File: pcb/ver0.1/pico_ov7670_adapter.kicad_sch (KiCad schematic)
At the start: 11 parts, among them J1 Conn_02x06_Odd_Even, SW1 SW_Push, U1 CAMERA-OV7670, U2 RASPBERRY_PI_PICO_W

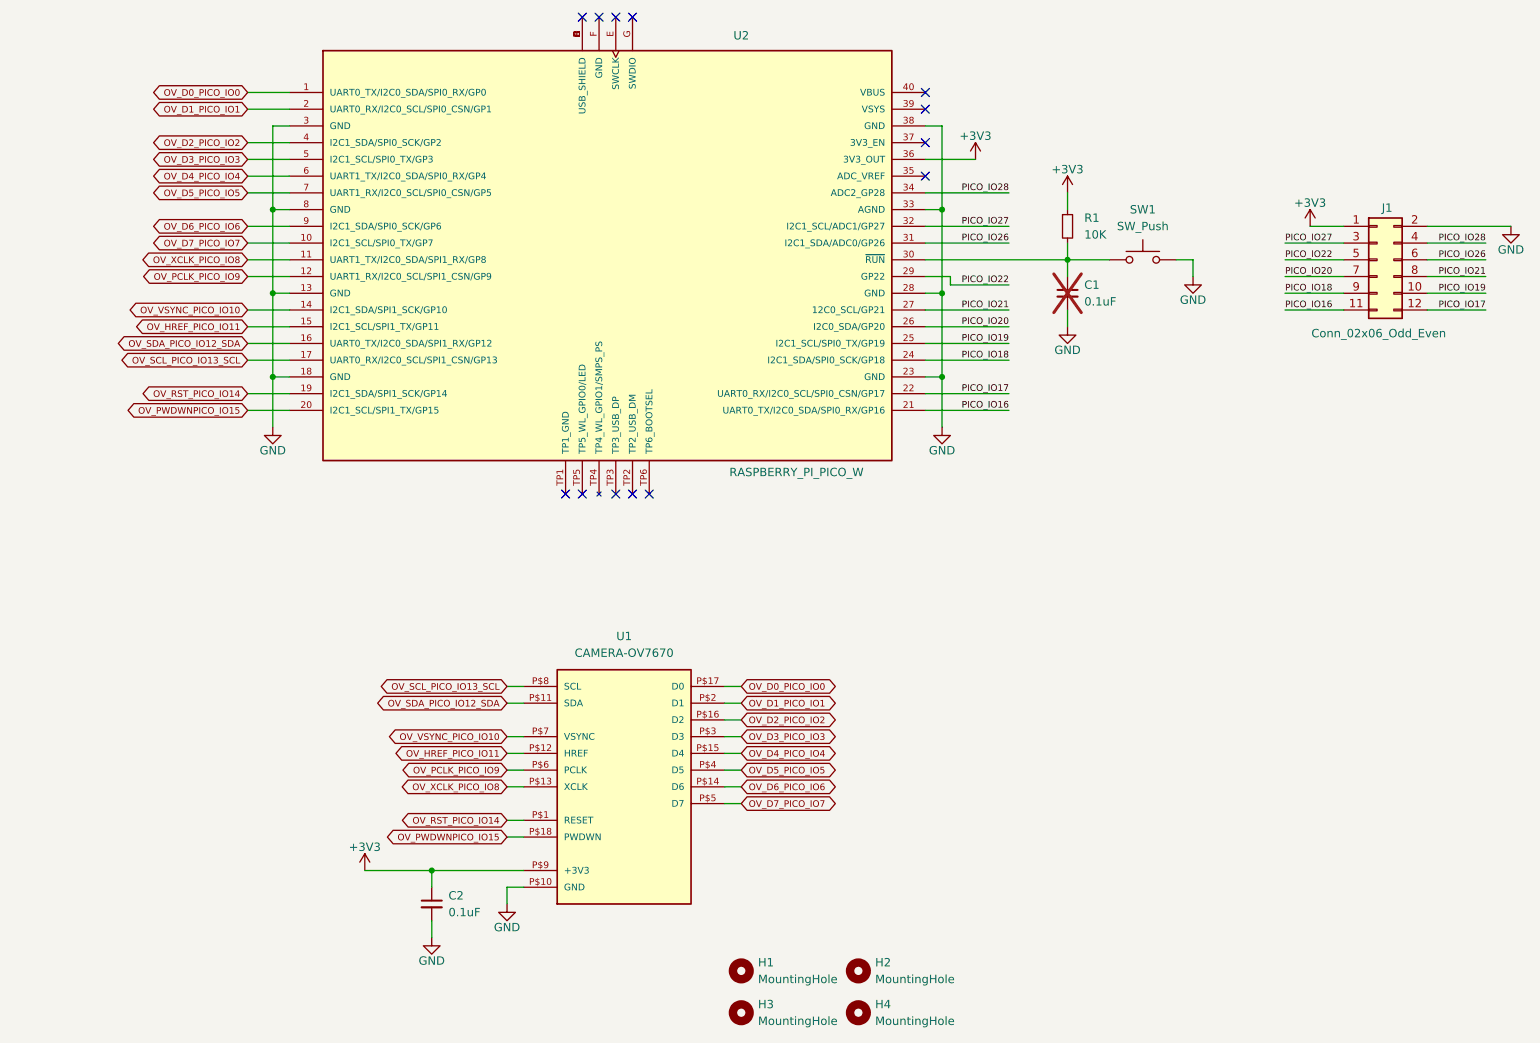
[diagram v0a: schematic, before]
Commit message: footprints updated
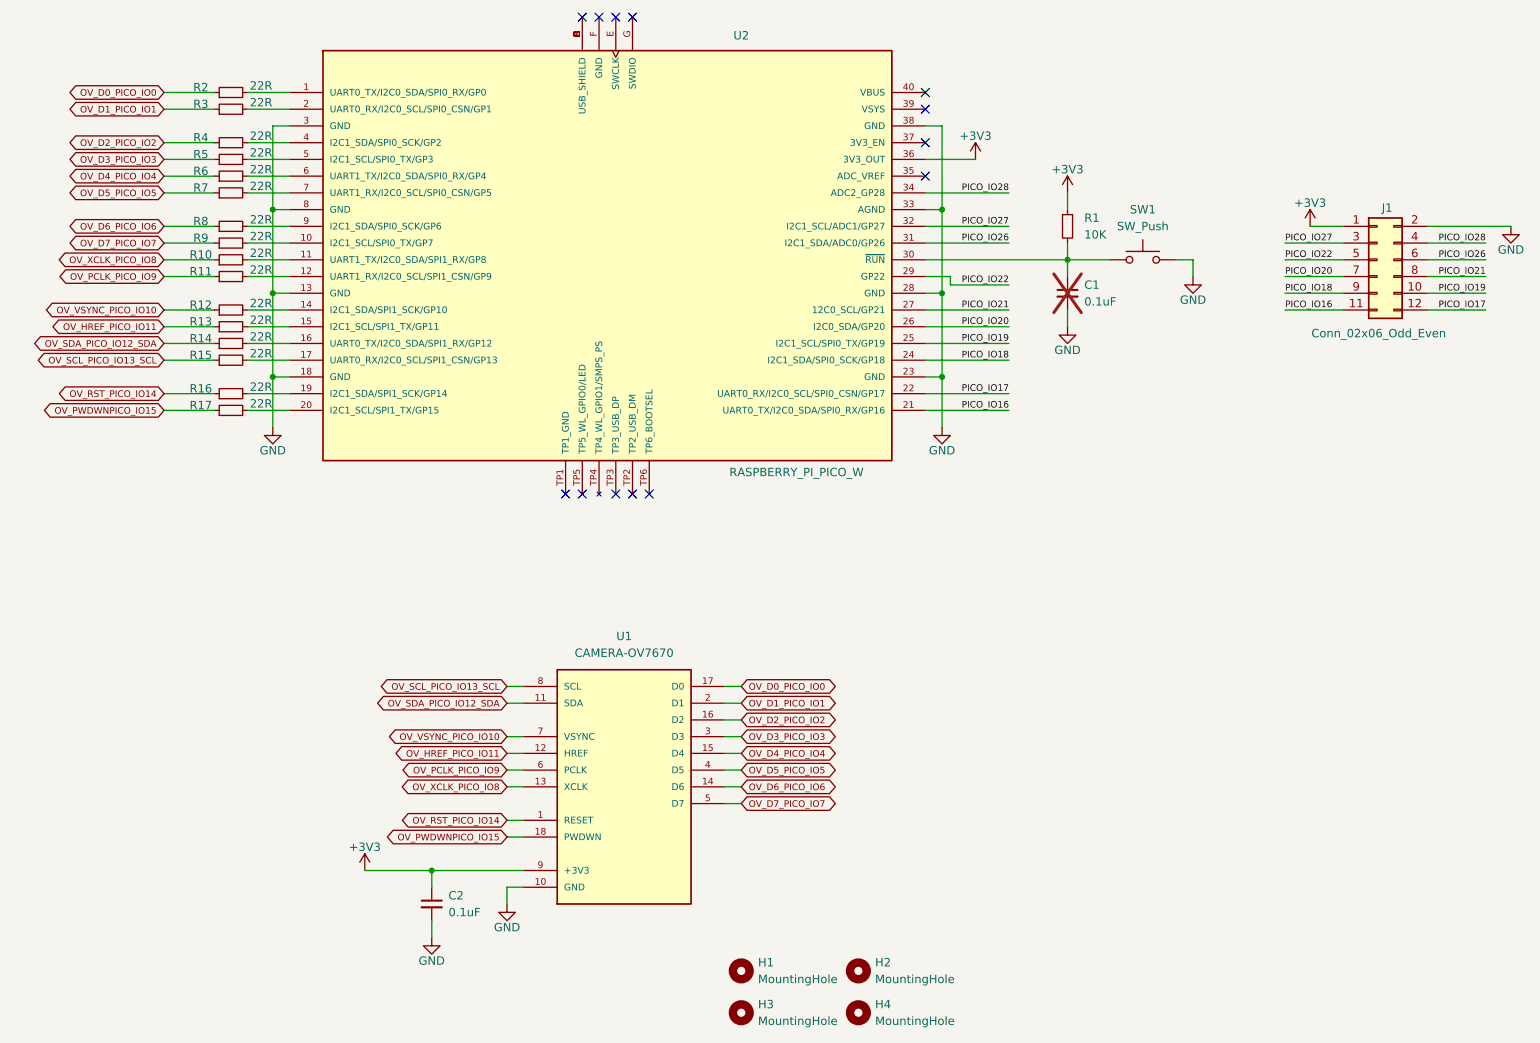
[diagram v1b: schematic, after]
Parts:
- added R10, R11, R12, R13, R14, R15, R16, R17, R2, R3, R4, R5, R6, R7, R8, R9: 22R, Resistor_SMD:R_0603_1608Metric, symbol Device:R_Small
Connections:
- net +3V3: now also U1.9 (+3V3); no longer U1.P$9 (+3V3)
- net GND: now also U1.10 (GND); no longer U1.P$10 (GND)
- net OV_D0_PICO_IO0: now also U1.17 (D0), R2.1; no longer U1.P$17 (D0), U2.1 (UART0_TX/I2C0_SDA/SPI0_RX/GP0)
- net OV_D1_PICO_IO1: now also U1.2 (D1), R3.1; no longer U1.P$2 (D1), U2.2 (UART0_RX/I2C0_SCL/SPI0_CSN/GP1)
- net OV_D2_PICO_IO2: now also U1.16 (D2), R4.1; no longer U1.P$16 (D2), U2.4 (I2C1_SDA/SPI0_SCK/GP2)
- net OV_D3_PICO_IO3: now also U1.3 (D3), R5.1; no longer U1.P$3 (D3), U2.5 (I2C1_SCL/SPI0_TX/GP3)
- net OV_D4_PICO_IO4: now also U1.15 (D4), R6.1; no longer U1.P$15 (D4), U2.6 (UART1_TX/I2C0_SDA/SPI0_RX/GP4)
- net OV_D5_PICO_IO5: now also U1.4 (D5), R7.1; no longer U1.P$4 (D5), U2.7 (UART1_RX/I2C0_SCL/SPI0_CSN/GP5)
- net OV_D6_PICO_IO6: now also U1.14 (D6), R8.1; no longer U1.P$14 (D6), U2.9 (I2C1_SDA/SPI0_SCK/GP6)
- net OV_D7_PICO_IO7: now also U1.5 (D7), R9.1; no longer U1.P$5 (D7), U2.10 (I2C1_SCL/SPI0_TX/GP7)
- net OV_HREF_PICO_IO11: now also U1.12 (HREF), R13.1; no longer U1.P$12 (HREF), U2.15 (I2C1_SCL/SPI1_TX/GP11)
- net OV_PCLK_PICO_IO9: now also U1.6 (PCLK), R11.1; no longer U1.P$6 (PCLK), U2.12 (UART1_RX/I2C0_SCL/SPI1_CSN/GP9)
- net OV_PWDWNPICO_IO15: now also U1.18 (PWDWN), R17.1; no longer U1.P$18 (PWDWN), U2.20 (I2C1_SCL/SPI1_TX/GP15)
- net OV_RST_PICO_IO14: now also U1.1 (RESET), R16.1; no longer U1.P$1 (RESET), U2.19 (I2C1_SDA/SPI1_SCK/GP14)
- net OV_SCL_PICO_IO13_SCL: now also U1.8 (SCL), R15.1; no longer U1.P$8 (SCL), U2.17 (UART0_RX/I2C0_SCL/SPI1_CSN/GP13)
- net OV_SDA_PICO_IO12_SDA: now also U1.11 (SDA), R14.1; no longer U1.P$11 (SDA), U2.16 (UART0_TX/I2C0_SDA/SPI1_RX/GP12)
- net OV_VSYNC_PICO_IO10: now also U1.7 (VSYNC), R12.1; no longer U1.P$7 (VSYNC), U2.14 (I2C1_SDA/SPI1_SCK/GP10)
- net OV_XCLK_PICO_IO8: now also U1.13 (XCLK), R10.1; no longer U1.P$13 (XCLK), U2.11 (UART1_TX/I2C0_SDA/SPI1_RX/GP8)
- new net: R6.2, U2.6 (UART1_TX/I2C0_SDA/SPI0_RX/GP4)
- new net: R15.2, U2.17 (UART0_RX/I2C0_SCL/SPI1_CSN/GP13)
- new net: R4.2, U2.4 (I2C1_SDA/SPI0_SCK/GP2)
- new net: R2.2, U2.1 (UART0_TX/I2C0_SDA/SPI0_RX/GP0)
- new net: R10.2, U2.11 (UART1_TX/I2C0_SDA/SPI1_RX/GP8)
- new net: R12.2, U2.14 (I2C1_SDA/SPI1_SCK/GP10)
- new net: R5.2, U2.5 (I2C1_SCL/SPI0_TX/GP3)
- new net: R16.2, U2.19 (I2C1_SDA/SPI1_SCK/GP14)
- new net: R9.2, U2.10 (I2C1_SCL/SPI0_TX/GP7)
- new net: R14.2, U2.16 (UART0_TX/I2C0_SDA/SPI1_RX/GP12)
- new net: R13.2, U2.15 (I2C1_SCL/SPI1_TX/GP11)
- new net: R7.2, U2.7 (UART1_RX/I2C0_SCL/SPI0_CSN/GP5)
- new net: R17.2, U2.20 (I2C1_SCL/SPI1_TX/GP15)
- new net: R11.2, U2.12 (UART1_RX/I2C0_SCL/SPI1_CSN/GP9)
- new net: R3.2, U2.2 (UART0_RX/I2C0_SCL/SPI0_CSN/GP1)
- new net: R8.2, U2.9 (I2C1_SDA/SPI0_SCK/GP6)
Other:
- title: PICO 2W OV7670 adapter board -> PICO OV7670 Adapter

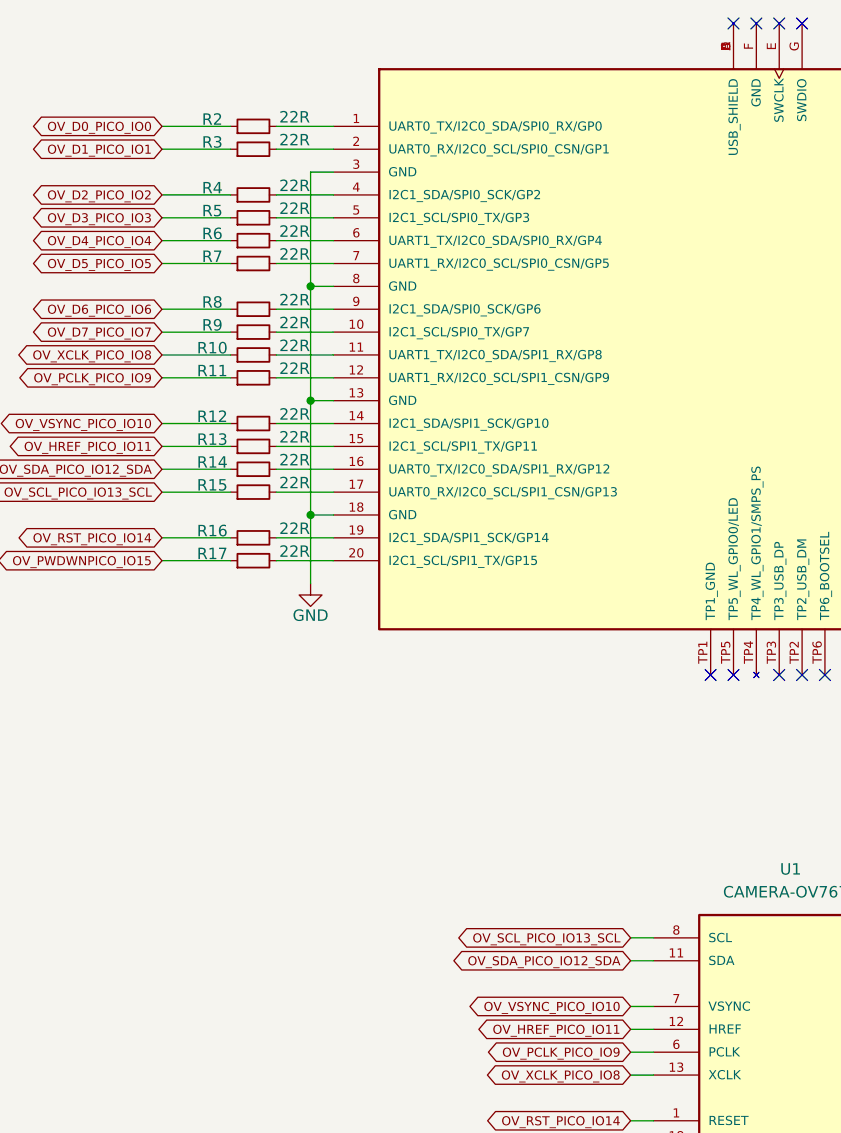
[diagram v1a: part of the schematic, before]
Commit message: layout updated
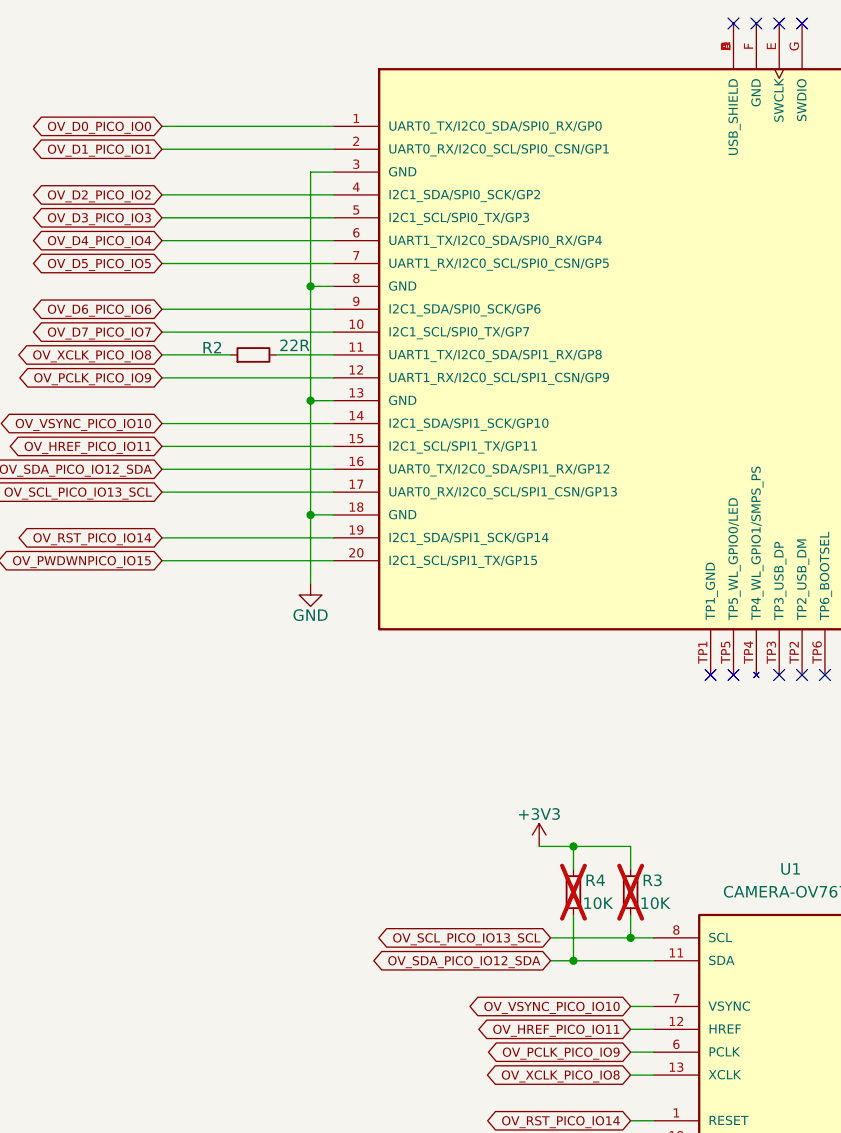
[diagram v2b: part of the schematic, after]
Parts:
- removed R10, R11, R12, R13, R14, R15, R16, R17, R5, R6, R7, R8, R9: 22R, Resistor_SMD:R_0603_1608Metric, symbol Device:R_Small
- R3, R4: value 22R -> 10K; now not fitted
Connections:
- net +3V3: now also R3.1, R4.1
- net OV_D0_PICO_IO0: now also U2.1 (UART0_TX/I2C0_SDA/SPI0_RX/GP0); no longer R2.1
- net OV_D1_PICO_IO1: now also U2.2 (UART0_RX/I2C0_SCL/SPI0_CSN/GP1); no longer R3.1
- net OV_D2_PICO_IO2: now also U2.4 (I2C1_SDA/SPI0_SCK/GP2); no longer R4.1
- net OV_D3_PICO_IO3: now also U2.5 (I2C1_SCL/SPI0_TX/GP3)
- net OV_D4_PICO_IO4: now also U2.6 (UART1_TX/I2C0_SDA/SPI0_RX/GP4)
- net OV_D5_PICO_IO5: now also U2.7 (UART1_RX/I2C0_SCL/SPI0_CSN/GP5)
- net OV_D6_PICO_IO6: now also U2.9 (I2C1_SDA/SPI0_SCK/GP6)
- net OV_D7_PICO_IO7: now also U2.10 (I2C1_SCL/SPI0_TX/GP7)
- net OV_HREF_PICO_IO11: now also U2.15 (I2C1_SCL/SPI1_TX/GP11)
- net OV_PCLK_PICO_IO9: now also U2.12 (UART1_RX/I2C0_SCL/SPI1_CSN/GP9)
- net OV_PWDWNPICO_IO15: now also U2.20 (I2C1_SCL/SPI1_TX/GP15)
- net OV_RST_PICO_IO14: now also U2.19 (I2C1_SDA/SPI1_SCK/GP14)
- net OV_SCL_PICO_IO13_SCL: now also R3.2, U2.17 (UART0_RX/I2C0_SCL/SPI1_CSN/GP13)
- net OV_SDA_PICO_IO12_SDA: now also R4.2, U2.16 (UART0_TX/I2C0_SDA/SPI1_RX/GP12)
- net OV_VSYNC_PICO_IO10: now also U2.14 (I2C1_SDA/SPI1_SCK/GP10)
- net OV_XCLK_PICO_IO8: now also R2.1
- net at R2.2: now also U2.11 (UART1_TX/I2C0_SDA/SPI1_RX/GP8); no longer U2.1 (UART0_TX/I2C0_SDA/SPI0_RX/GP0)

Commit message: basic routing completed
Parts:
- removed J1: Conn_02x06_Odd_Even, Connector_PinSocket_2.54mm:PinSocket_2x06_P2.54mm_Vertical, symbol Connector_Generic:Conn_02x06_Odd_Even
- added C3: 0.1uF, Capacitor_SMD:C_0603_1608Metric, symbol Device:C_Small
- added J1: GPIO Header, Connector_PinHeader_2.54mm:PinHeader_2x05_P2.54mm_Vertical, symbol Connector_Generic:Conn_02x05_Odd_Even
- added R5: 10K, Resistor_SMD:R_0603_1608Metric, symbol Device:R_Small
- added SW2: SW_Push, Button_Switch_SMD:SW_SPST_PTS810, symbol Switch:SW_Push
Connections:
- net +3V3: now also J1.1 (Pin_1), R5.1
- net GND: now also C3.2, J1.2 (Pin_2), J1.3 (Pin_3), SW2.2
- net OV_HREF_PICO_IO11: now also U2.14 (I2C1_SDA/SPI1_SCK/GP10); no longer U2.15 (I2C1_SCL/SPI1_TX/GP11)
- net OV_PCLK_PICO_IO9: now also U2.17 (UART0_RX/I2C0_SCL/SPI1_CSN/GP13); no longer U2.12 (UART1_RX/I2C0_SCL/SPI1_CSN/GP9)
- net OV_RST_PICO_IO14: now also U2.20 (I2C1_SCL/SPI1_TX/GP15); no longer U2.19 (I2C1_SDA/SPI1_SCK/GP14)
- net OV_SCL_PICO_IO13_SCL: now also U2.12 (UART1_RX/I2C0_SCL/SPI1_CSN/GP9); no longer U2.17 (UART0_RX/I2C0_SCL/SPI1_CSN/GP13)
- net OV_SDA_PICO_IO12_SDA: now also U2.11 (UART1_TX/I2C0_SDA/SPI1_RX/GP8); no longer U2.16 (UART0_TX/I2C0_SDA/SPI1_RX/GP12)
- net OV_VSYNC_PICO_IO10: now also U2.15 (I2C1_SCL/SPI1_TX/GP11); no longer U2.14 (I2C1_SDA/SPI1_SCK/GP10)
- net PICO_IO19: now also J1.4 (Pin_4)
- net PICO_IO20: now also J1.6 (Pin_6)
- net PICO_IO21: now also J1.5 (Pin_5)
- net PICO_IO22: now also J1.8 (Pin_8)
- net PICO_IO26: now also J1.7 (Pin_7)
- net PICO_IO27: now also J1.10 (Pin_10)
- net PICO_IO28: now also J1.9 (Pin_9)
- net PICO_RESET: now reaches C1.1, R1.2, SW1.1, U2.30 (~{RUN})
- net at R2.2: now also U2.16 (UART0_TX/I2C0_SDA/SPI1_RX/GP12); no longer U2.11 (UART1_TX/I2C0_SDA/SPI1_RX/GP8)
- net OV_PWDWNPICO_IO15 renamed OV_PWDWN_PICO_IO15
- net OV_PWDWN_PICO_IO15: now also U2.19 (I2C1_SDA/SPI1_SCK/GP14); no longer U2.20 (I2C1_SCL/SPI1_TX/GP15)
- net PICO_IO16: no longer names the net of U2.21 (UART0_TX/I2C0_SDA/SPI0_RX/GP16)
- net PICO_IO17: no longer names the net of U2.22 (UART0_RX/I2C0_SCL/SPI0_CSN/GP17)
- net PICO_IO18 renamed USER_Button
- net USER_Button: now also C3.1, R5.2, SW2.1
- no-connect marks 13 -> 15
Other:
- moved on the sheet: R2

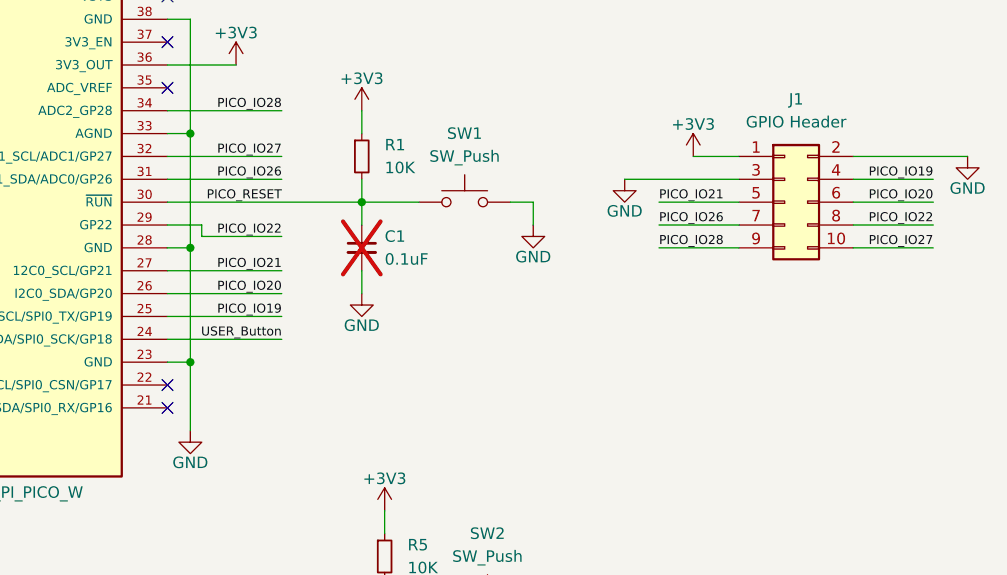
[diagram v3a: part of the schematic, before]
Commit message: art work updated in PCB
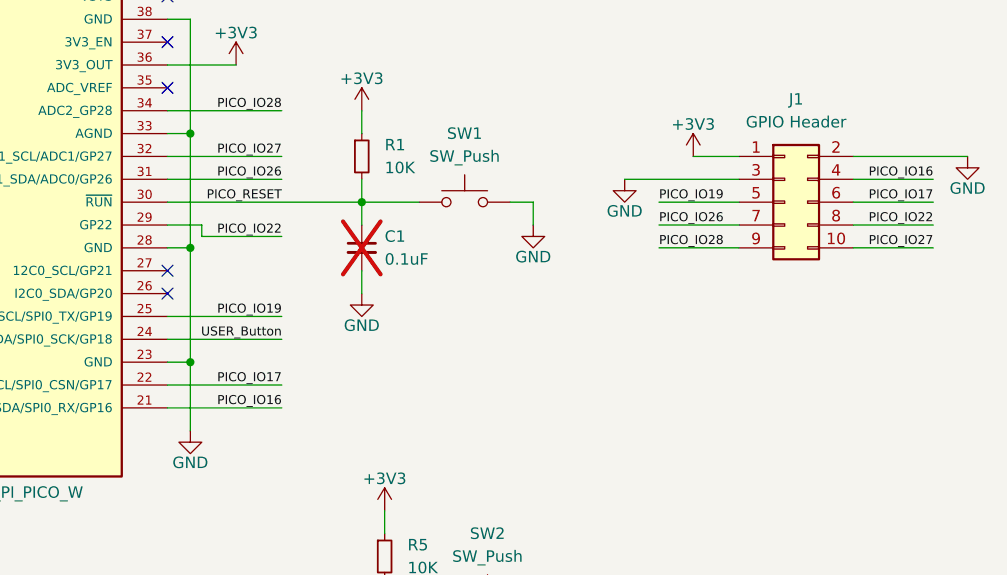
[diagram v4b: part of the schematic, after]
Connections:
- net PICO_IO19: now also J1.5 (Pin_5); no longer J1.4 (Pin_4)
- net PICO_IO16: now reaches U2.21 (UART0_TX/I2C0_SDA/SPI0_RX/GP16)
- net PICO_IO16: now also J1.4 (Pin_4)
- net PICO_IO17: now reaches U2.22 (UART0_RX/I2C0_SCL/SPI0_CSN/GP17)
- net PICO_IO17: now also J1.6 (Pin_6)
- net PICO_IO20: no longer names the net of U2.26 (I2C0_SDA/GP20)
- net PICO_IO20: no longer J1.6 (Pin_6)
- net PICO_IO21: no longer names the net of U2.27 (12C0_SCL/GP21)
- net PICO_IO21: no longer J1.5 (Pin_5)
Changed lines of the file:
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@@
 	)
 	(no_connect
-		(at 167.64 99.06)
+		(at 167.64 86.36)
 	)
 	(no_connect
@@
 	)
 	(no_connect
-		(at 167.64 96.52)
+		(at 167.64 83.82)
 	)
 	(no_connect
@@
 	(wire
 		(pts
+			(xy 167.64 99.06) (xy 180.34 99.06)
+		)
+		(stroke
+			(width 0)
+			(type default)
+		)
+	)
+	(wire
+		(pts
 			(xy 68.58 68.58) (xy 71.12 68.58)
 		)
@@
 	(wire
 		(pts
-			(xy 167.64 83.82) (xy 180.34 83.82)
-		)
-		(stroke
-			(width 0)
-			(type default)
-		)
-	)
-	(wire
-		(pts
 			(xy 52.07 83.82) (xy 71.12 83.82)
 		)
@@
 	(wire
 		(pts
-			(xy 167.64 86.36) (xy 180.34 86.36)
-		)
-		(stroke
-			(width 0)
-			(type default)
-		)
-	)
-	(wire
-		(pts
 			(xy 243.84 76.2) (xy 252.73 76.2)
 		)
@@
 		(pts
 			(xy 68.58 93.98) (xy 71.12 93.98)
+		)
+		(stroke
+			(width 0)
+			(type default)
+		)
+	)
+	(wire
+		(pts
+			(xy 167.64 96.52) (xy 180.34 96.52)
 		)
 		(stroke
@@
 		)
 	)
-	(label "PICO_IO21"
-		(at 180.34 83.82 180)
-		(fields_autoplaced yes)
-		(effects
-			(font
-				(size 1 1)
-			)
-			(justify right bottom)
-		)
-	)
-	(label "PICO_IO20"
+	(label "PICO_IO17"
+		(at 180.34 96.52 180)
+		(fields_autoplaced yes)
+		(effects
+			(font
+				(size 1 1)
+			)
+			(justify right bottom)
+		)
+	)
+	(label "PICO_IO17"
 		(at 252.73 76.2 180)
+		(fields_autoplaced yes)
+		(effects
+			(font
+				(size 1 1)
+			)
+			(justify right bottom)
+		)
+	)
+	(label "PICO_IO16"
+		(at 252.73 73.66 180)
 		(fields_autoplaced yes)
 		(effects
@@
 	)
 	(label "PICO_IO19"
-		(at 252.73 73.66 180)
-		(fields_autoplaced yes)
-		(effects
-			(font
-				(size 1 1)
-			)
-			(justify right bottom)
+		(at 222.25 76.2 0)
+		(fields_autoplaced yes)
+		(effects
+			(font
+				(size 1 1)
+			)
+			(justify left bottom)
 		)
 	)
@@
 		)
 	)
-	(label "PICO_IO20"
-		(at 180.34 86.36 180)
+	(label "PICO_IO16"
+		(at 180.34 99.06 180)
 		(fields_autoplaced yes)
 		(effects
@@
 		)
 	)
-	(label "PICO_IO21"
-		(at 222.25 76.2 0)
-		(fields_autoplaced yes)
-		(effects
-			(font
-				(size 1 1)
-			)
-			(justify left bottom)
-		)
-	)

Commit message: via stitching added
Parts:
- C1, C3, R3, R4: now fitted
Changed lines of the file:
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@@
 		(in_bom yes)
 		(on_board yes)
-		(dnp yes)
+		(dnp no)
 		(property "Reference" "R3"
 			(at 105.41 134.62 0)
@@
 		(in_bom yes)
 		(on_board yes)
-		(dnp yes)
+		(dnp no)
 		(fields_autoplaced yes)
 		(property "Reference" "C3"
@@
 		(in_bom yes)
 		(on_board yes)
-		(dnp yes)
+		(dnp no)
 		(fields_autoplaced yes)
 		(property "Reference" "C1"
@@
 		(in_bom yes)
 		(on_board yes)
-		(dnp yes)
+		(dnp no)
 		(property "Reference" "R4"
 			(at 99.06 134.62 0)
